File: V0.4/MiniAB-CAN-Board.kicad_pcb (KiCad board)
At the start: 4 copper layers, 51.1 x 45.2 mm, 128 parts, among them J1 PCF, J10 USB_B_Micro, J11 CAN, J12 ENDSTOP1, J13 ENDSTOP2, J14 PROBE, J2 PCF, J3 HEF, J4 TH0, J5 I2C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

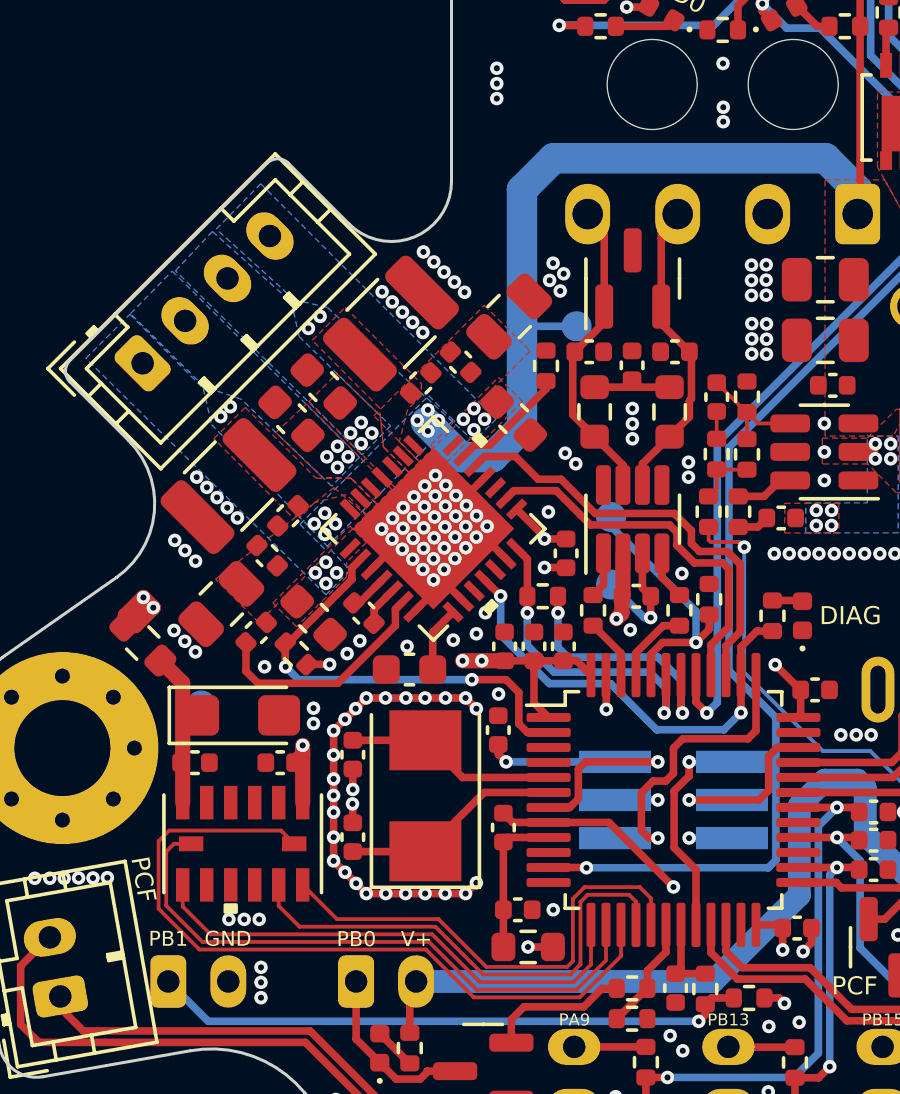
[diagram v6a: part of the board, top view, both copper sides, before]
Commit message: Add step models for CAD export
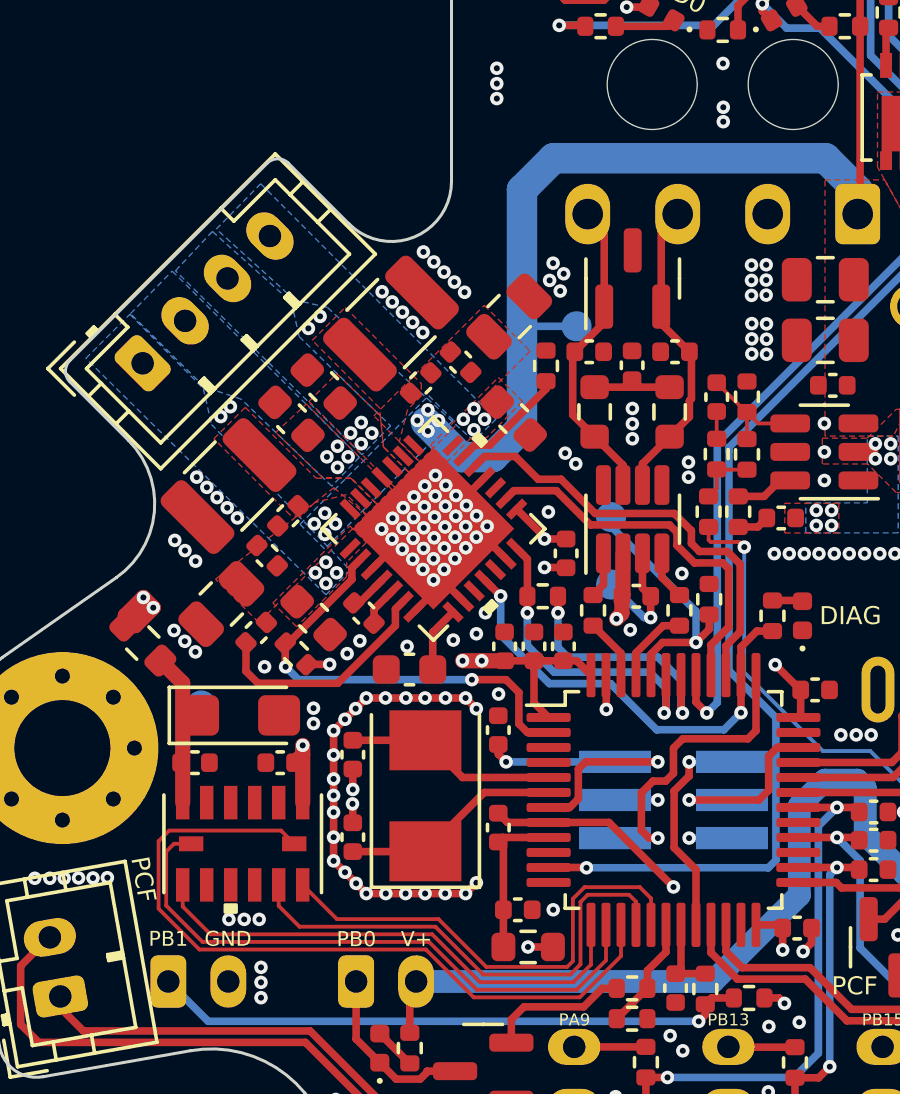
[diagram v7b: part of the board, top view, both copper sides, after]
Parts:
- moved C12 0.17 mm to (206.5, 74.4)
